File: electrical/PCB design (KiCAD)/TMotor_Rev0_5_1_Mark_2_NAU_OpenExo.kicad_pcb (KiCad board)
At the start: 2 copper layers, 89.4 x 82.6 mm, 96 parts, among them J1 Conn_01x07_Pin, J10 XT30PW-F, J11 XT30PW-F, J12 XT30PW-F, J13 TFM-107-01-L-D-WT, J2 Conn_01x04_Pin, J3 Conn_01x02_Pin, J4 Conn_01x02_Pin, J5 Conn_01x02_Pin, J6 Conn_01x02_Pin, J7 Conn_01x03_Pin, J8 XT30PW-F, J9 XT30PW-F, U1 TXU0104PWR, U10 DEV-16771, U2 TXU0304-Q1, U3 INA125U, U4 INA125U, U5 SN65HVD230DR, U6 INA125U, U7 INA125U

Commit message: design updates ; documentation update
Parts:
- removed the C19 at (157.9, 124.8)
- removed the C26 at (119.5, 71.7)
- removed the C3 at (151.7, 106.5)
- removed the D1 at (140.6, 121.3)
- removed D3, D4, D5: BAT54S, Package_TO_SOT_SMD:SOT-23
- removed INA_EXC_JP6, INA_EXC_JP7: SolderJumper_3_Open, Jumper:SolderJumper-3_P1.3mm_Open_RoundedPad1.0x1.5mm_NumberLabels
- removed J1: Conn_01x07_Pin, Connector_PinHeader_2.54mm:PinHeader_1x07_P2.54mm_Vertical
- removed J12: XT30PW-F, XT30PW-F:AMASS_XT30U-F_1x02_P5.0mm_Vertical
- removed the J4 at (136.6, 130.0)
- removed PS1: P78E05-1000, TMotor_Rev0_5_1_Mark_2_NAU_OpenExo:P78E05-1000
- removed the RIGHT_LC_CONN1 at (156.1, 69.9)
- removed U10: DEV-16771, TMotor_Rev0_5_1_Mark_2_NAU_OpenExo:MODULE_DEV-16771
- added C10: 22uF, Capacitor_SMD:C_0805_2012Metric_Pad1.18x1.45mm_HandSolder, B.Cu at (164.4, 117.0)
- added C11: 22uF, Capacitor_SMD:C_0805_2012Metric_Pad1.18x1.45mm_HandSolder, B.Cu at (164.4, 114.7)
- added C13: 100nF, Capacitor_SMD:C_0805_2012Metric_Pad1.18x1.45mm_HandSolder, F.Cu at (162.4, 132.5)
- added C23: 100nF, Capacitor_SMD:C_0805_2012Metric_Pad1.18x1.45mm_HandSolder, F.Cu at (144.5, 70.6)
- added C25: 1uF, Capacitor_SMD:C_0805_2012Metric_Pad1.18x1.45mm_HandSolder, F.Cu at (146.6, 70.6)
- added C28: 100nF, Capacitor_SMD:C_0805_2012Metric_Pad1.18x1.45mm_HandSolder, F.Cu at (124.0, 65.9)
- added C30: 1uF, Capacitor_SMD:C_0805_2012Metric_Pad1.18x1.45mm_HandSolder, F.Cu at (121.8, 65.9)
- added C32: 10nF, Capacitor_SMD:C_0805_2012Metric_Pad1.18x1.45mm_HandSolder, F.Cu at (152.3, 127.1)
- added C33: 10nF, Capacitor_SMD:C_0805_2012Metric_Pad1.18x1.45mm_HandSolder, F.Cu at (143.9, 111.7)
- added C34: 10nF, Capacitor_SMD:C_0805_2012Metric_Pad1.18x1.45mm_HandSolder, F.Cu at (141.2, 104.8)
- added C35: 10nF, Capacitor_SMD:C_0805_2012Metric_Pad1.18x1.45mm_HandSolder, F.Cu at (144.7, 99.5)
- added C36: 10nF, Capacitor_SMD:C_0805_2012Metric_Pad1.18x1.45mm_HandSolder, B.Cu at (155.3, 124.0)
- added C37: 10nF, Capacitor_SMD:C_0805_2012Metric_Pad1.18x1.45mm_HandSolder, F.Cu at (143.9, 109.5)
- added C38: 10nF, Capacitor_SMD:C_0805_2012Metric_Pad1.18x1.45mm_HandSolder, F.Cu at (142.6, 99.4)
- added C39: 10nF, Capacitor_SMD:C_0805_2012Metric_Pad1.18x1.45mm_HandSolder, F.Cu at (145.2, 95.2)
- added D10: BAS70-04, BAS70-04:P200_SOT-23, F.Cu at (152.7, 97.6)
- added D7: BAS70-04, BAS70-04:P200_SOT-23, B.Cu at (143.8, 117.0)
- added D8: BAS70-04, BAS70-04:P200_SOT-23, F.Cu at (150.9, 113.4)
- added D9: BAS70-04, BAS70-04:P200_SOT-23, F.Cu at (151.1, 108.5)
- added INA_EXC_JP1: SolderJumper_2_Open, Jumper:SolderJumper-2_P1.3mm_Open_RoundedPad1.0x1.5mm, F.Cu at (136.4, 134.2)
- added INA_EXC_JP2: SolderJumper_2_Open, Jumper:SolderJumper-2_P1.3mm_Open_RoundedPad1.0x1.5mm, F.Cu at (160.3, 126.5)
- added J7: XT30PW-F, XT30 new version:AMASS_XT30U-F_1x02_P5.0mm_Vertical, F.Cu at (182.4, 68.5)
- added R22: 1k, Resistor_SMD:R_0805_2012Metric_Pad1.20x1.40mm_HandSolder, B.Cu at (159.5, 124.0)
- added R23: 1k, Resistor_SMD:R_0805_2012Metric_Pad1.20x1.40mm_HandSolder, F.Cu at (133.8, 131.9)
- added R24: 1k, Resistor_SMD:R_0805_2012Metric_Pad1.20x1.40mm_HandSolder, B.Cu at (140.4, 84.2)
- added R25: 1k, Resistor_SMD:R_0805_2012Metric_Pad1.20x1.40mm_HandSolder, B.Cu at (125.3, 78.9)
- added RIGHT_LC_CONN2: TFM-107-01-L-D-WT, ISDF connector:SAMTEC_TFM-107-01-L-D-WT, F.Cu at (106.8, 114.5)
- added U7: DEV-16771, TEENSY:MODULE_DEV-16771, F.Cu at (120.2, 104.5)
- added U9: WPME-FDSM_SIP-3, 173010535:WPME-FDSM_17301XX35, F.Cu at (163.0, 113.0)
- C1: renamed from C6; footprint Capacitor_THT:C_Disc_D10.5mm_W5.0mm_P5.00mm -> Capacitor_SMD:C_0805_2012Metric_Pad1.18x1.45mm_HandSolder; moved to B.Cu
- C14: renamed from C24; footprint Capacitor_THT:C_Disc_D10.5mm_W5.0mm_P5.00mm -> Capacitor_SMD:C_0805_2012Metric_Pad1.18x1.45mm_HandSolder; moved to B.Cu
- C15: value 100nF -> 1uF; footprint Capacitor_THT:C_Disc_D10.5mm_W5.0mm_P5.00mm -> Capacitor_SMD:C_0805_2012Metric_Pad1.18x1.45mm_HandSolder
- C16: renamed from C25; footprint Capacitor_THT:C_Disc_D10.5mm_W5.0mm_P5.00mm -> Capacitor_SMD:C_0805_2012Metric_Pad1.18x1.45mm_HandSolder; moved to B.Cu
- C18, C2: footprint Capacitor_THT:C_Disc_D10.5mm_W5.0mm_P5.00mm -> Capacitor_SMD:C_0805_2012Metric_Pad1.18x1.45mm_HandSolder; moved to B.Cu
- C19: renamed from C21; footprint Capacitor_THT:C_Disc_D10.5mm_W5.0mm_P5.00mm -> Capacitor_SMD:C_0805_2012Metric_Pad1.18x1.45mm_HandSolder
- C20: value 100nF -> 1uF; footprint Capacitor_THT:C_Disc_D10.5mm_W5.0mm_P5.00mm -> Capacitor_SMD:C_0805_2012Metric_Pad1.18x1.45mm_HandSolder; moved to B.Cu
- C21: renamed from C22; footprint Capacitor_THT:C_Disc_D10.5mm_W5.0mm_P5.00mm -> Capacitor_SMD:C_0805_2012Metric_Pad1.18x1.45mm_HandSolder; moved to B.Cu
- C24: renamed from C27; footprint Capacitor_THT:C_Disc_D10.5mm_W5.0mm_P5.00mm -> Capacitor_SMD:C_0805_2012Metric_Pad1.18x1.45mm_HandSolder
- C26: renamed from C29; footprint Capacitor_THT:C_Disc_D10.5mm_W5.0mm_P5.00mm -> Capacitor_SMD:C_0805_2012Metric_Pad1.18x1.45mm_HandSolder
- C29: renamed from C28; footprint Capacitor_THT:C_Disc_D10.5mm_W5.0mm_P5.00mm -> Capacitor_SMD:C_0805_2012Metric_Pad1.18x1.45mm_HandSolder
- C3: renamed from C8; footprint Capacitor_THT:C_Disc_D10.5mm_W5.0mm_P5.00mm -> Capacitor_SMD:C_0805_2012Metric_Pad1.18x1.45mm_HandSolder; moved to B.Cu
- C31: renamed from C30; footprint Capacitor_THT:C_Disc_D10.5mm_W5.0mm_P5.00mm -> Capacitor_SMD:C_0805_2012Metric_Pad1.18x1.45mm_HandSolder
- C4: renamed from C7; footprint Capacitor_THT:C_Disc_D10.5mm_W5.0mm_P5.00mm -> Capacitor_SMD:C_0805_2012Metric_Pad1.18x1.45mm_HandSolder; moved to B.Cu
- C5: renamed from C23; footprint Capacitor_THT:C_Disc_D10.5mm_W5.0mm_P5.00mm -> Capacitor_SMD:C_0805_2012Metric_Pad1.18x1.45mm_HandSolder; moved to B.Cu
- C6: renamed from C5; footprint Capacitor_THT:C_Disc_D10.5mm_W5.0mm_P5.00mm -> Capacitor_SMD:C_0805_2012Metric_Pad1.18x1.45mm_HandSolder; moved to B.Cu
- C7: renamed from C9; footprint Capacitor_THT:C_Disc_D10.5mm_W5.0mm_P5.00mm -> Capacitor_SMD:C_0805_2012Metric_Pad1.18x1.45mm_HandSolder; moved to B.Cu
- C9: renamed from C4; footprint Capacitor_THT:C_Disc_D10.5mm_W5.0mm_P5.00mm -> Capacitor_SMD:C_0805_2012Metric_Pad1.18x1.45mm_HandSolder; moved to B.Cu
- INA_EXC_JP3, INA_EXC_JP4: value SolderJumper_3_Open -> SolderJumper_2_Open; footprint Jumper:SolderJumper-3_P1.3mm_Open_RoundedPad1.0x1.5mm_NumberLabels -> Jumper:SolderJumper-2_P1.3mm_Open_RoundedPad1.0x1.5mm
- INA_PWR_JP4: moved to F.Cu
- J10, J11, J8, J9: footprint XT30PW-F:AMASS_XT30U-F_1x02_P5.0mm_Vertical -> XT30 new version:AMASS_XT30U-F_1x02_P5.0mm_Vertical
- LEFT_LC_CONN1: value CONN_04X2 -> TFM-107-01-L-D-WT; footprint Connector_PinHeader_2.54mm:PinHeader_2x04_P2.54mm_Vertical -> ISDF connector:SAMTEC_TFM-107-01-L-D-WT
- R1: renamed from R12; footprint Resistor_THT:R_Axial_DIN0207_L6.3mm_D2.5mm_P10.16mm_Horizontal -> Resistor_SMD:R_0805_2012Metric_Pad1.20x1.40mm_HandSolder; moved to B.Cu
- R10: renamed from R4; value 4.7k -> 1k; footprint Resistor_THT:R_Axial_DIN0207_L6.3mm_D2.5mm_P10.16mm_Horizontal -> Resistor_SMD:R_0805_2012Metric_Pad1.20x1.40mm_HandSolder; moved to B.Cu
- R11: renamed from R15; value 10R -> 50; footprint Resistor_THT:R_Axial_DIN0207_L6.3mm_D2.5mm_P10.16mm_Horizontal -> Resistor_SMD:R_0805_2012Metric_Pad1.20x1.40mm_HandSolder
- R12: renamed from R20; value 1M -> 100k; footprint Resistor_THT:R_Axial_DIN0207_L6.3mm_D2.5mm_P10.16mm_Horizontal -> Resistor_SMD:R_0805_2012Metric_Pad1.20x1.40mm_HandSolder; moved to B.Cu
- R13: renamed from R24; value 1M -> 100k; footprint Resistor_THT:R_Axial_DIN0207_L6.3mm_D2.5mm_P10.16mm_Horizontal -> Resistor_SMD:R_0805_2012Metric_Pad1.20x1.40mm_HandSolder
- R14: renamed from R5; value 4.7k -> 1k; footprint Resistor_THT:R_Axial_DIN0207_L6.3mm_D2.5mm_P10.16mm_Horizontal -> Resistor_SMD:R_0805_2012Metric_Pad1.20x1.40mm_HandSolder; moved to B.Cu
- R15: renamed from R17; value 10R -> 50; footprint Resistor_THT:R_Axial_DIN0207_L6.3mm_D2.5mm_P10.16mm_Horizontal -> Resistor_SMD:R_0805_2012Metric_Pad1.20x1.40mm_HandSolder; moved to B.Cu
- R16: renamed from R21; value 1M -> 100k; footprint Resistor_THT:R_Axial_DIN0207_L6.3mm_D2.5mm_P10.16mm_Horizontal -> Resistor_SMD:R_0805_2012Metric_Pad1.20x1.40mm_HandSolder
- R17: renamed from R25; value 1M -> 100k; footprint Resistor_THT:R_Axial_DIN0207_L6.3mm_D2.5mm_P10.16mm_Horizontal -> Resistor_SMD:R_0805_2012Metric_Pad1.20x1.40mm_HandSolder
- R18: renamed from R6; value 4.7k -> 1k; footprint Resistor_THT:R_Axial_DIN0207_L6.3mm_D2.5mm_P10.16mm_Horizontal -> Resistor_SMD:R_0805_2012Metric_Pad1.20x1.40mm_HandSolder; moved to B.Cu
- R19: renamed from R18; value 10R -> 50; footprint Resistor_THT:R_Axial_DIN0207_L6.3mm_D2.5mm_P10.16mm_Horizontal -> Resistor_SMD:R_0805_2012Metric_Pad1.20x1.40mm_HandSolder; moved to B.Cu
- R2: renamed from R1; footprint Resistor_THT:R_Axial_DIN0207_L6.3mm_D2.5mm_P10.16mm_Horizontal -> Resistor_SMD:R_0805_2012Metric_Pad1.20x1.40mm_HandSolder; moved to B.Cu
- R20: renamed from R22; value 1M -> 100k; footprint Resistor_THT:R_Axial_DIN0207_L6.3mm_D2.5mm_P10.16mm_Horizontal -> Resistor_SMD:R_0805_2012Metric_Pad1.20x1.40mm_HandSolder
- R21: renamed from R26; value 1M -> 100k; footprint Resistor_THT:R_Axial_DIN0207_L6.3mm_D2.5mm_P10.16mm_Horizontal -> Resistor_SMD:R_0805_2012Metric_Pad1.20x1.40mm_HandSolder
- R3: renamed from R2; value 10R -> 10; footprint Resistor_THT:R_Axial_DIN0207_L6.3mm_D2.5mm_P10.16mm_Horizontal -> Resistor_SMD:R_0805_2012Metric_Pad1.20x1.40mm_HandSolder
- R4: renamed from R11; footprint Resistor_THT:R_Axial_DIN0207_L6.3mm_D2.5mm_P10.16mm_Horizontal -> Resistor_SMD:R_0805_2012Metric_Pad1.20x1.40mm_HandSolder
- R5: renamed from R7; footprint Resistor_THT:R_Axial_DIN0207_L6.3mm_D2.5mm_P10.16mm_Horizontal -> Resistor_SMD:R_0805_2012Metric_Pad1.20x1.40mm_HandSolder
- R6: renamed from R3; value 4.7k -> 1k; footprint Resistor_THT:R_Axial_DIN0207_L6.3mm_D2.5mm_P10.16mm_Horizontal -> Resistor_SMD:R_0805_2012Metric_Pad1.20x1.40mm_HandSolder
- R7: renamed from R16; value 10R -> 50; footprint Resistor_THT:R_Axial_DIN0207_L6.3mm_D2.5mm_P10.16mm_Horizontal -> Resistor_SMD:R_0805_2012Metric_Pad1.20x1.40mm_HandSolder; moved to B.Cu
- R8: renamed from R19; value 1M -> 100k; footprint Resistor_THT:R_Axial_DIN0207_L6.3mm_D2.5mm_P10.16mm_Horizontal -> Resistor_SMD:R_0805_2012Metric_Pad1.20x1.40mm_HandSolder; moved to B.Cu
- R9: renamed from R23; value 1M -> 100k; footprint Resistor_THT:R_Axial_DIN0207_L6.3mm_D2.5mm_P10.16mm_Horizontal -> Resistor_SMD:R_0805_2012Metric_Pad1.20x1.40mm_HandSolder; moved to B.Cu
- moved RIGHT_LC_CONN1 87.6 mm to (160.0, 67.6)
- moved C20 73.2 mm to (134.1, 142.6), turned to -90 degrees
- moved INA_EXC_JP3 66.9 mm to (136.3, 73.3)
- moved J9 48.6 mm to (184.1, 117.1)
- moved R8 43.1 mm to (162.1, 138.6), turned to 0 degrees
- moved C15 23.5 mm to (162.0, 136.4), turned to 180 degrees
- moved R11 23.1 mm to (145.5, 140.9), turned to -90 degrees
- moved R21 23.0 mm to (137.6, 69.5), turned to 0 degrees
- moved R20 22.8 mm to (137.6, 66.1), turned to 0 degrees
- moved R17 20.7 mm to (157.0, 72.8), turned to 0 degrees
- moved C3 20.2 mm to (124.4, 107.8), turned to -90 degrees
- moved J10 20.0 mm to (189.3, 136.3)
- moved R5 19.3 mm to (147.4, 130.2)
- moved R13 19.0 mm to (147.6, 144.1), turned to -90 degrees
- moved C18 16.9 mm to (134.2, 138.2), turned to 90 degrees
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- renumbered C1 to C8, D2 to D1, D6 to D2, INA219 to INA1, INA_PWR_JP3 to INA_PWR_JP1, INA_PWR_JP6 to INA_PWR_JP2, INA_PWR_JP7 to INA_PWR_JP3, INA_VREF_JP3 to INA_VREF_JP1, INA_VREF_JP6 to INA_VREF_JP2, INA_VREF_JP7 to INA_VREF_JP3, J6 to J3, J5 to J4, J3 to J5, J7 to J6, J13 to RIGHT_LC_CONN1, SHUNT0 to SHUNT1, TP2 to TP1, TP1 to TP2, U$6 to U$1, U3 to U1, U6 to U2, U7 to U3, U1 to U5, U2 to U6, U5 to U8
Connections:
- A1 pad D0: /MCUs/NANO_RX -> /MCUs/NANO_TX
- C14 pad 1: /Load cells/Left LC Amplifier 2/Vbridge- -> /Load cells/Left LC Amplifier 2 (label 2)/Vbridge-
- C15 pad 1: Net-(PS1-GND/-VOUT) -> Net-(INA_PWR_JP2-C)
- C16 pad 1: /Load cells/Left LC Amplifier 2/Vbridge+ -> /Load cells/Left LC Amplifier 2 (label 2)/Vbridge+
- C18 pad 1: Net-(U3-SENSE) (its old number) -> Net-(INA_PWR_JP1-C)
- C19 pad 1: /Load cells/Left LC  Amplifier 1/Vbridge- -> /Load cells/Left LC  Amplifier 1 (label 1)/Vbridge-
- C20 pad 1: Net-(U4-SENSE) -> Net-(INA_PWR_JP1-C)
- C21 pad 1: /Load cells/Left LC  Amplifier 1/Vbridge+ -> /Load cells/Left LC  Amplifier 1 (label 1)/Vbridge+
- C24 pad 1: /Load cells/Right LC  Amplifier 2/Vbridge- -> /Load cells/Right LC  Amplifier 2 (label 4)/Vbridge-
- C26 pad 1: /Load cells/Right LC  Amplifier 2/Vbridge+ -> /Load cells/Right LC  Amplifier 2 (label 4)/Vbridge+
- C29 pad 1: /Load cells/Right LC Amplifier 1/Vbridge- -> /Load cells/Right LC Amplifier 1 (label 3)/Vbridge-
- C31 pad 1: /Load cells/Right LC Amplifier 1/Vbridge+ -> /Load cells/Right LC Amplifier 1 (label 3)/Vbridge+
- INA_EXC_JP3 pad 1: +5V -> Net-(INA_EXC_JP3-A)
- INA_EXC_JP3 pad 2: L1_LC_P -> Net-(INA_EXC_JP3-B)
- INA_EXC_JP4 pad 1: +5V -> Net-(INA_EXC_JP4-A)
- INA_EXC_JP4 pad 2: R2_LC_P -> Net-(INA_EXC_JP4-B)
- INA_PWR_JP1 pad 2: Net-(INA_PWR_JP3-C) (its old number) -> Net-(INA_PWR_JP1-C)
- INA_PWR_JP2 pad 2: Net-(INA_PWR_JP6-C) -> Net-(INA_PWR_JP2-C)
- INA_VREF_JP1 pad 2: Net-(INA_EXC_JP3-B) -> Net-(INA_EXC_JP1-A)
- INA_VREF_JP3 pad 2: Net-(INA_EXC_JP7-B) -> Net-(INA_EXC_JP3-A)
- INA_VREF_JP4 pad 2: Net-(INA_EXC_JP4-B) -> Net-(INA_EXC_JP4-A)
- J10 pad 1: (no net) -> GND
- J10 pad 2: (no net) -> /CAN and peripherals./VBATT
- J11 pad 1: (no net) -> GND
- J11 pad 2: (no net) -> /CAN and peripherals./VBATT
- J8 pad 1: (no net) -> GND
- J8 pad 2: (no net) -> /CAN and peripherals./VBATT
- J9 pad 1: (no net) -> GND
- J9 pad 2: (no net) -> /CAN and peripherals./VBATT
- R10 pad 1: Net-(U3-SENSE) (its old number) -> Net-(U1-SENSE)
- R12 pad 1: /Load cells/Left LC  Amplifier 1/Vbridge+ -> /Load cells/Left LC  Amplifier 1 (label 1)/Vbridge+
- R13 pad 1: /Load cells/Left LC  Amplifier 1/Vbridge- -> /Load cells/Left LC  Amplifier 1 (label 1)/Vbridge-
- R16 pad 1: /Load cells/Right LC  Amplifier 2/Vbridge+ -> /Load cells/Right LC  Amplifier 2 (label 4)/Vbridge+
- R17 pad 1: /Load cells/Right LC  Amplifier 2/Vbridge- -> /Load cells/Right LC  Amplifier 2 (label 4)/Vbridge-
- R20 pad 1: /Load cells/Right LC Amplifier 1/Vbridge+ -> /Load cells/Right LC Amplifier 1 (label 3)/Vbridge+
- R21 pad 1: /Load cells/Right LC Amplifier 1/Vbridge- -> /Load cells/Right LC Amplifier 1 (label 3)/Vbridge-
- R8 pad 1: /Load cells/Left LC Amplifier 2/Vbridge+ -> /Load cells/Left LC Amplifier 2 (label 2)/Vbridge+
- R9 pad 1: /Load cells/Left LC Amplifier 2/Vbridge- -> /Load cells/Left LC Amplifier 2 (label 2)/Vbridge-
- RIGHT_LC_CONN1 pad 01: unconnected-(J13-Pad01) -> /Load cells/Right LC  Amplifier 2 (label 4)/Vbridge+
- RIGHT_LC_CONN1 pad 02: unconnected-(J13-Pad02) -> /Load cells/Right LC Amplifier 1 (label 3)/Vbridge-
- RIGHT_LC_CONN1 pad 03: unconnected-(J13-Pad03) -> /Load cells/Right LC  Amplifier 2 (label 4)/Vbridge-
- RIGHT_LC_CONN1 pad 04: unconnected-(J13-Pad04) -> /Load cells/Right LC Amplifier 1 (label 3)/Vbridge+
- RIGHT_LC_CONN1 pad 05: unconnected-(J13-Pad05) -> +5V
- RIGHT_LC_CONN1 pad 06: unconnected-(J13-Pad06) -> GND
- RIGHT_LC_CONN1 pad 07: unconnected-(J13-Pad07) -> +5V
- RIGHT_LC_CONN1 pad 08: unconnected-(J13-Pad08) -> GND
- TeensyPowerJP1 pad 1: +5V -> Net-(TeensyPowerJP1-A)
- TeensyPowerJP1 pad 2: Net-(TeensyPowerJP1-B) -> +5V
- U$1 pad 1: Net-(PS1-GND/-VOUT) -> Net-(U$1-P$1)
- U1 pad 1: Net-(INA_PWR_JP3-C) (its old number) -> Net-(INA_PWR_JP1-C)
- U1 pad 10: Net-(U3-SENSE) (its old number) -> Net-(U1-SENSE)
- U1 pad 11: Net-(U3-SENSE) (its old number) -> Net-(U1-SENSE)
- U1 pad 2: Net-(INA_PWR_JP3-C) (its old number) -> Net-(INA_PWR_JP1-C)
- U1 pad 4: Net-(INA_EXC_JP3-B) -> Net-(INA_EXC_JP1-A)
- U1 pad 5: Net-(INA_EXC_JP3-B) -> Net-(INA_EXC_JP1-A)
- U1 pad 6: /Load cells/Left LC  Amplifier 1/Vbridge+ -> /Load cells/Left LC  Amplifier 1 (label 1)/Vbridge+
- U1 pad 7: /Load cells/Left LC  Amplifier 1/Vbridge- -> /Load cells/Left LC  Amplifier 1 (label 1)/Vbridge-
- U2 pad 1: Net-(INA_PWR_JP6-C) -> Net-(INA_PWR_JP2-C)
- U2 pad 2: Net-(INA_PWR_JP6-C) -> Net-(INA_PWR_JP2-C)
- U2 pad 6: /Load cells/Left LC Amplifier 2/Vbridge+ -> /Load cells/Left LC Amplifier 2 (label 2)/Vbridge+
- U2 pad 7: /Load cells/Left LC Amplifier 2/Vbridge- -> /Load cells/Left LC Amplifier 2 (label 2)/Vbridge-
- U3 pad 4: Net-(INA_EXC_JP7-B) -> Net-(INA_EXC_JP3-A)
- U3 pad 5: Net-(INA_EXC_JP7-B) -> Net-(INA_EXC_JP3-A)
- U3 pad 6: /Load cells/Right LC Amplifier 1/Vbridge+ -> /Load cells/Right LC Amplifier 1 (label 3)/Vbridge+
- U3 pad 7: /Load cells/Right LC Amplifier 1/Vbridge- -> /Load cells/Right LC Amplifier 1 (label 3)/Vbridge-
- U4 pad 4: Net-(INA_EXC_JP4-B) -> Net-(INA_EXC_JP4-A)
- U4 pad 5: Net-(INA_EXC_JP4-B) -> Net-(INA_EXC_JP4-A)
- U4 pad 6: /Load cells/Right LC  Amplifier 2/Vbridge+ -> /Load cells/Right LC  Amplifier 2 (label 4)/Vbridge+
- U4 pad 7: /Load cells/Right LC  Amplifier 2/Vbridge- -> /Load cells/Right LC  Amplifier 2 (label 4)/Vbridge-
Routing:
- net /Load cells/Right LC Amplifier 1/Vbridge+: track 55.2 -> 0.00 mm, vias 2 -> 0
- net /Load cells/Right LC Amplifier 1/Vbridge-: track 52.1 -> 0.00 mm, vias 1 -> 0
- net /Load cells/Left LC Amplifier 2/Vbridge+: track 50.9 -> 0.00 mm
- net /Load cells/Left LC  Amplifier 1/Vbridge+: track 47.8 -> 0.00 mm, vias 1 -> 0
- net /Load cells/Left LC  Amplifier 1/Vbridge-: track 42.4 -> 0.00 mm, vias 1 -> 0
- net /Load cells/Right LC  Amplifier 2/Vbridge-: track 35.6 -> 0.00 mm, vias 1 -> 0
- net /Load cells/Right LC Amplifier 1 (label 3)/Vbridge+: track 0.00 -> 32.9 mm, vias 0 -> 1
- net /Load cells/Right LC  Amplifier 2/Vbridge+: track 32.9 -> 0.00 mm, vias 1 -> 0
- net /Load cells/Right LC Amplifier 1 (label 3)/Vbridge-: track 0.00 -> 29.7 mm, vias 0 -> 1
- net Net-(U3-SENSE) (its old number): track 26.8 -> 0.00 mm, vias 1 -> 0
- net /Load cells/Left LC Amplifier 2/Vbridge-: track 22.0 -> 0.00 mm
- net R2_LC_P: track 50.2 -> 28.5 mm
- net /Load cells/Left LC  Amplifier 1 (label 1)/Vbridge-: track 0.00 -> 21.6 mm, vias 0 -> 1
- net /Load cells/Left LC  Amplifier 1 (label 1)/Vbridge+: track 0.00 -> 20.9 mm, vias 0 -> 3
- net SYNC_DEFAULT: track 20.1 -> 0.00 mm
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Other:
- board text added: "AnkleExo Board v1.1.1 McGill NeuroC Lab (2026)"
- board text added: "INA_PWR"
- board text added: "SPI"
- board text removed: "AnkleExo Board v1.1.0 McGill NeuroC Lab (2026)"
- board text removed: "CIPO"
- board text removed: "COPI"
- board text removed: "CS1"
- board text removed: "CS2"
- board text removed: "INAPwr"
- board text removed: "INARef"
- board text removed: "SCK"
- board text removed: "SPIx2"

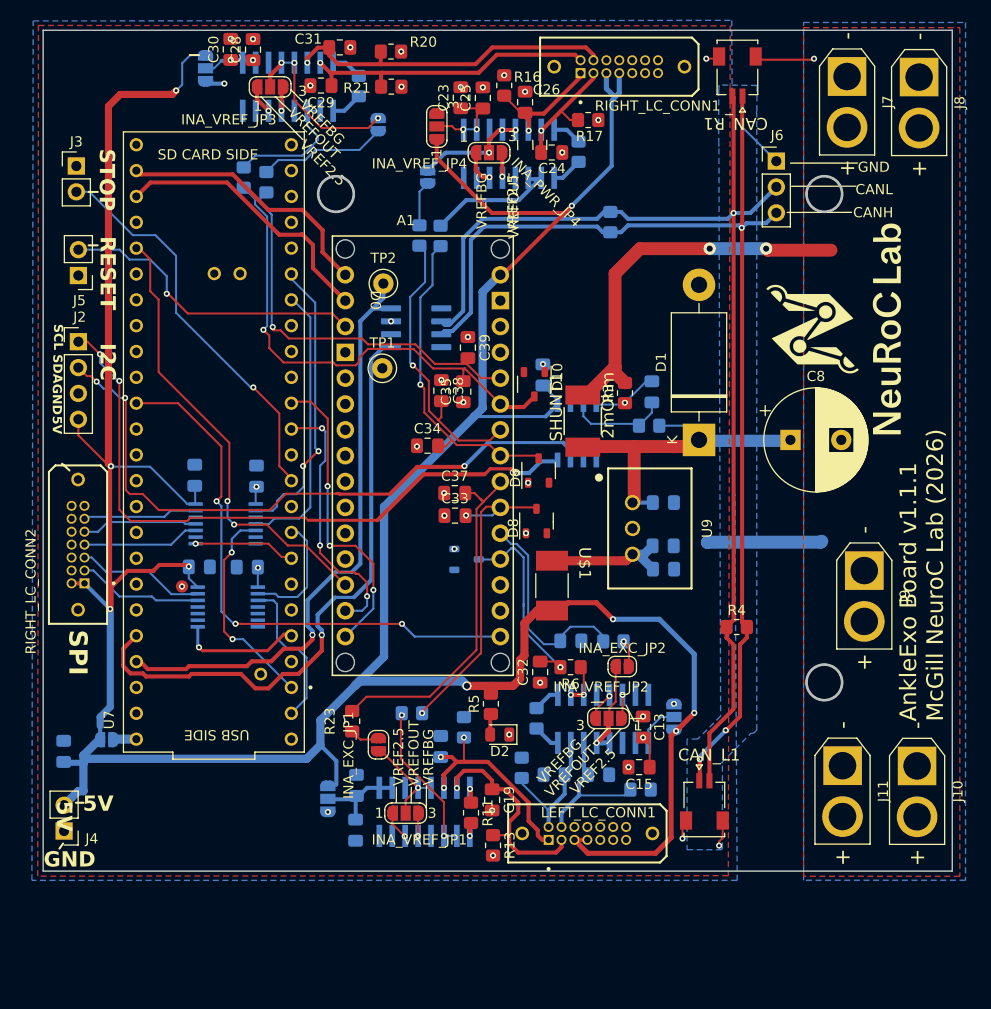
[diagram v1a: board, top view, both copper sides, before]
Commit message: updated ble and uart
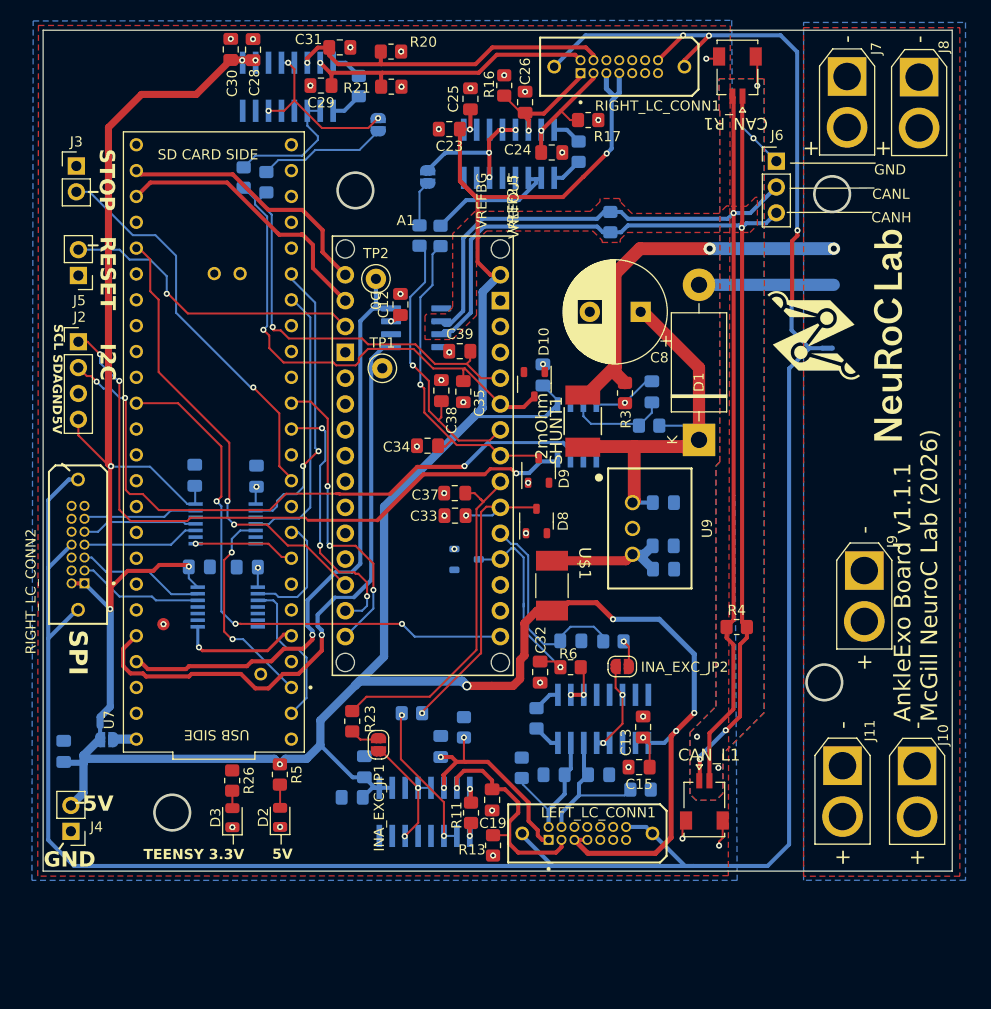
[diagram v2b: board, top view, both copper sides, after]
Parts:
- removed INA_PWR_JP1, INA_PWR_JP2, INA_PWR_JP3, INA_PWR_JP4, INA_VREF_JP1, INA_VREF_JP2, INA_VREF_JP3, INA_VREF_JP4: SolderJumper_3_Open, Jumper:SolderJumper-3_P1.3mm_Open_RoundedPad1.0x1.5mm_NumberLabels
- added C12: 100nF, Capacitor_SMD:C_0805_2012Metric_Pad1.18x1.45mm_HandSolder, F.Cu at (138.5, 90.9)
- added D3: LED, LED_SMD:LED_0805_2012Metric, F.Cu at (122.0, 141.4)
- added NT1: NetTie_2, NetTie:NetTie-2_SMD_Pad0.5mm, B.Cu at (180.5, 95.2)
- added R26: 470, Resistor_SMD:R_0805_2012Metric_Pad1.20x1.40mm_HandSolder, F.Cu at (122.0, 137.7)
- R5: value 600kR -> 1k
- moved D2 23.1 mm to (126.7, 141.4), turned to 90 degrees
- moved R5 21.9 mm to (126.7, 137.1), turned to -90 degrees
- moved C8 19.4 mm to (162.1, 91.7), turned to 180 degrees
- moved C20 6.29 mm to (135.0, 136.4), turned to 90 degrees
- moved C23 3.28 mm to (143.3, 73.7), turned to 180 degrees
- moved C18 1.25 mm to (133.8, 139.4), turned to 180 degrees
- moved C25 1.22 mm to (145.4, 70.7)
- moved C39 0.87 mm to (144.4, 95.5), turned to 0 degrees
- moved TP2 0.86 mm to (136.1, 88.4)
- moved J4 0.67 mm to (106.1, 142.7)
- moved G*** 0.62 mm to (181.6, 94.0)
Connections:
- C13 pad 1: Net-(INA_PWR_JP2-C) -> +5V
- C15 pad 1: Net-(INA_PWR_JP2-C) -> +5V
- C18 pad 1: Net-(INA_PWR_JP1-C) -> +5V
- C20 pad 1: Net-(INA_PWR_JP1-C) -> +5V
- C23 pad 1: Net-(INA_PWR_JP4-C) -> +5V
- C25 pad 1: Net-(INA_PWR_JP4-C) -> +5V
- C28 pad 1: Net-(INA_PWR_JP3-C) -> +5V
- C30 pad 1: Net-(INA_PWR_JP3-C) -> +5V
- LEFT_LC_CONN1 pad 14: unconnected-(LEFT_LC_CONN1-Pad14) -> SHIELD
- LEFT_LC_CONN1 pad S1: (no net) -> SHIELD
- LEFT_LC_CONN1 pad S2: (no net) -> SHIELD
- R5 pad 1: Net-(D2-A) -> +5V
- R5 pad 2: +5V -> Net-(D2-A)
- RIGHT_LC_CONN1 pad 14: unconnected-(RIGHT_LC_CONN1-Pad14) -> SHIELD
- RIGHT_LC_CONN1 pad S1: (no net) -> SHIELD
- RIGHT_LC_CONN1 pad S2: (no net) -> SHIELD
- RIGHT_LC_CONN2 pad 08: unconnected-(RIGHT_LC_CONN2-Pad08) -> SHIELD
- RIGHT_LC_CONN2 pad S1: (no net) -> SHIELD
- RIGHT_LC_CONN2 pad S2: (no net) -> SHIELD
- U1 pad 1: Net-(INA_PWR_JP1-C) -> +5V
- U1 pad 13: Net-(INA_VREF_JP1-B) -> unconnected-(U1-VREFBG-Pad13)
- U1 pad 14: Net-(INA_VREF_JP1-A) -> Net-(INA_EXC_JP1-A)
- U1 pad 2: Net-(INA_PWR_JP1-C) -> +5V
- U2 pad 1: Net-(INA_PWR_JP2-C) -> +5V
- U2 pad 13: Net-(INA_VREF_JP2-B) -> unconnected-(U2-VREFBG-Pad13)
- U2 pad 14: Net-(INA_VREF_JP2-A) -> Net-(INA_EXC_JP2-A)
- U2 pad 2: Net-(INA_PWR_JP2-C) -> +5V
- U3 pad 1: Net-(INA_PWR_JP3-C) -> +5V
- U3 pad 13: Net-(INA_VREF_JP3-B) -> unconnected-(U3-VREFBG-Pad13)
- U3 pad 14: Net-(INA_VREF_JP3-A) -> Net-(INA_EXC_JP3-A)
- U3 pad 2: Net-(INA_PWR_JP3-C) -> +5V
- U4 pad 1: Net-(INA_PWR_JP4-C) -> +5V
- U4 pad 13: Net-(INA_VREF_JP4-B) -> unconnected-(U4-VREFBG-Pad13)
- U4 pad 14: Net-(INA_VREF_JP4-A) -> Net-(INA_EXC_JP4-A)
- U4 pad 2: Net-(INA_PWR_JP4-C) -> +5V
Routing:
- net SHIELD: track 0.00 -> 246.8 mm, vias 0 -> 4
- net +5V: track 330.0 -> 350.4 mm, vias 9 -> 13
- net Net-(INA_PWR_JP2-C): track 9.22 -> 0.00 mm, vias 1 -> 0
- net Net-(INA_PWR_JP1-C): track 8.82 -> 0.00 mm
- net Net-(INA_PWR_JP4-C): track 8.54 -> 0.00 mm, vias 2 -> 0
- net /CAN and peripherals./L7_VIN: track 33.5 -> 41.1 mm
- net Net-(INA_PWR_JP3-C): track 5.37 -> 0.00 mm, vias 2 -> 0
- net Net-(INA_VREF_JP4-A): track 3.36 -> 0.00 mm, vias 1 -> 0
- net Net-(INA_VREF_JP3-A): track 2.82 -> 0.00 mm, vias 1 -> 0
- net Net-(INA_VREF_JP1-A): track 2.78 -> 0.00 mm, vias 1 -> 0
- net Net-(INA_VREF_JP2-B): track 2.74 -> 0.00 mm, vias 1 -> 0
- net Net-(INA_EXC_JP4-A): track 11.0 -> 13.4 mm, vias 3 -> 4
- net Net-(INA_VREF_JP3-B): track 2.43 -> 0.00 mm, vias 1 -> 0
- net Net-(INA_VREF_JP4-B): track 2.35 -> 0.00 mm, vias 1 -> 0
- net Net-(INA_VREF_JP2-A): track 2.33 -> 0.00 mm, vias 1 -> 0
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- added copper zone on F.Cu, net GND
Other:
- outline, holes or cut-outs redrawn
- board text added: "TEENSY 3.3V"
- board text removed: "3.3V"
- board text removed: "3V3"
- board text removed: "INA125 V+"
- board text removed: "INA_PWR"
- board text removed: "INA_pwr"

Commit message: fix modularize python script for ble.py and sensors.py (main and plotting-csv not done
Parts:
- removed INA1: ~, TMotor_Rev0_5_1_Mark_2_NAU_OpenExo:D8_TEX
- removed J6: Conn_01x03_Pin, Connector_PinHeader_2.54mm:PinHeader_1x03_P2.54mm_Vertical
- added C17: 0.1uF, Capacitor_SMD:C_0805_2012Metric_Pad1.18x1.45mm_HandSolder, B.Cu at (160.2, 104.5)
- added C22: 0.1uF, Capacitor_SMD:C_0805_2012Metric_Pad1.18x1.45mm_HandSolder, F.Cu at (166.4, 76.0)
- added C27: 10nF, Capacitor_SMD:C_0805_2012Metric_Pad1.18x1.45mm_HandSolder, F.Cu at (121.1, 85.5)
- added C40: 10nF, Capacitor_SMD:C_0805_2012Metric_Pad1.18x1.45mm_HandSolder, F.Cu at (121.2, 83.5)
- added J1: Conn_02x03_Counter_Clockwise, Connector_PinHeader_2.54mm:PinHeader_2x03_P2.54mm_Vertical, F.Cu at (174.9, 77.7)
- added JP1: SolderJumper_3_Open, Jumper:SolderJumper-3_P1.3mm_Open_RoundedPad1.0x1.5mm, B.Cu at (168.8, 70.4)
- added JP2: SolderJumper_3_Open, Jumper:SolderJumper-3_P1.3mm_Open_RoundedPad1.0x1.5mm, B.Cu at (150.9, 66.8)
- added R27: 3.3k, Resistor_SMD:R_0805_2012Metric_Pad1.20x1.40mm_HandSolder, B.Cu at (151.8, 102.7)
- added R28: 3.3k, Resistor_SMD:R_0805_2012Metric_Pad1.20x1.40mm_HandSolder, B.Cu at (151.8, 104.8)
- added R29: 10k, Resistor_THT:R_Axial_DIN0207_L6.3mm_D2.5mm_P7.62mm_Horizontal, F.Cu at (163.3, 72.3)
- added R30: 10k, Resistor_THT:R_Axial_DIN0207_L6.3mm_D2.5mm_P7.62mm_Horizontal, F.Cu at (166.4, 72.3)
- added R31: 1k, Resistor_SMD:R_0805_2012Metric_Pad1.20x1.40mm_HandSolder, B.Cu at (125.9, 86.8)
- added R32: 1k, Resistor_SMD:R_0805_2012Metric_Pad1.20x1.40mm_HandSolder, B.Cu at (123.9, 85.1)
- added U10: INA232AIDDFR, INA232AIDDFR:SOT_32AIDDFR_TEX, B.Cu at (156.4, 102.4)
- C6: value 100nF -> 0.1uF; moved to F.Cu
- C7: value 100nF -> 0.1uF
- R2: value 10R -> 10
- moved C6 24.5 mm to (163.3, 75.9), turned to -90 degrees
- moved R2 0.55 mm to (163.5, 102.8)
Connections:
- C6 pad 1: +5V -> FSR_2_IN
- RIGHT_LC_CONN1 pad 10: unconnected-(RIGHT_LC_CONN1-Pad10) -> /Load cells/FSR1/Vexcitation
- RIGHT_LC_CONN1 pad 11: unconnected-(RIGHT_LC_CONN1-Pad11) -> FSR_2_IN
- RIGHT_LC_CONN1 pad 12: unconnected-(RIGHT_LC_CONN1-Pad12) -> FSR_1_IN
- RIGHT_LC_CONN1 pad 13: unconnected-(RIGHT_LC_CONN1-Pad13) -> /Load cells/FSR2/Vexcitation
- U7 pad 18: unconnected-(U7-A4-Pad18) -> SDA
- U7 pad 19: unconnected-(U7-A5-Pad19) -> SCL
- U7 pad 24: unconnected-(U7-A10-Pad24) -> Net-(U7-A10)
- U7 pad 25: unconnected-(U7-A11-Pad25) -> Net-(U7-A11)
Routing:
- net FSR_1_IN: track 0.00 -> 63.0 mm
- net FSR_2_IN: track 0.00 -> 53.2 mm
- net Net-(U7-A10): track 0.00 -> 13.2 mm, vias 0 -> 1
- net /Load cells/FSR1/Vexcitation: track 0.00 -> 12.6 mm, vias 0 -> 1
- net Net-(U7-A11): track 0.00 -> 12.6 mm, vias 0 -> 1
- net +3V3: track 4.49 -> 11.7 mm, vias 4 -> 9
- net SCL: track 65.0 -> 72.2 mm
- net /Load cells/FSR2/Vexcitation: track 0.00 -> 5.95 mm, vias 0 -> 1
- net GND: track 27.6 -> 33.0 mm, vias 37 -> 41
- net +5V: track 350.4 -> 354.6 mm, vias 13 -> 14
- net R1_LC_P: track 39.9 -> 43.5 mm
- net SDA: track 63.5 -> 66.7 mm
- net R1_LC_N: track 48.9 -> 51.5 mm
- net Net-(U10-IN-): track 9.76 -> 7.66 mm
- net /CAN and peripherals./CAN_P: track 113.0 -> 114.6 mm
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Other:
- outline, holes or cut-outs redrawn

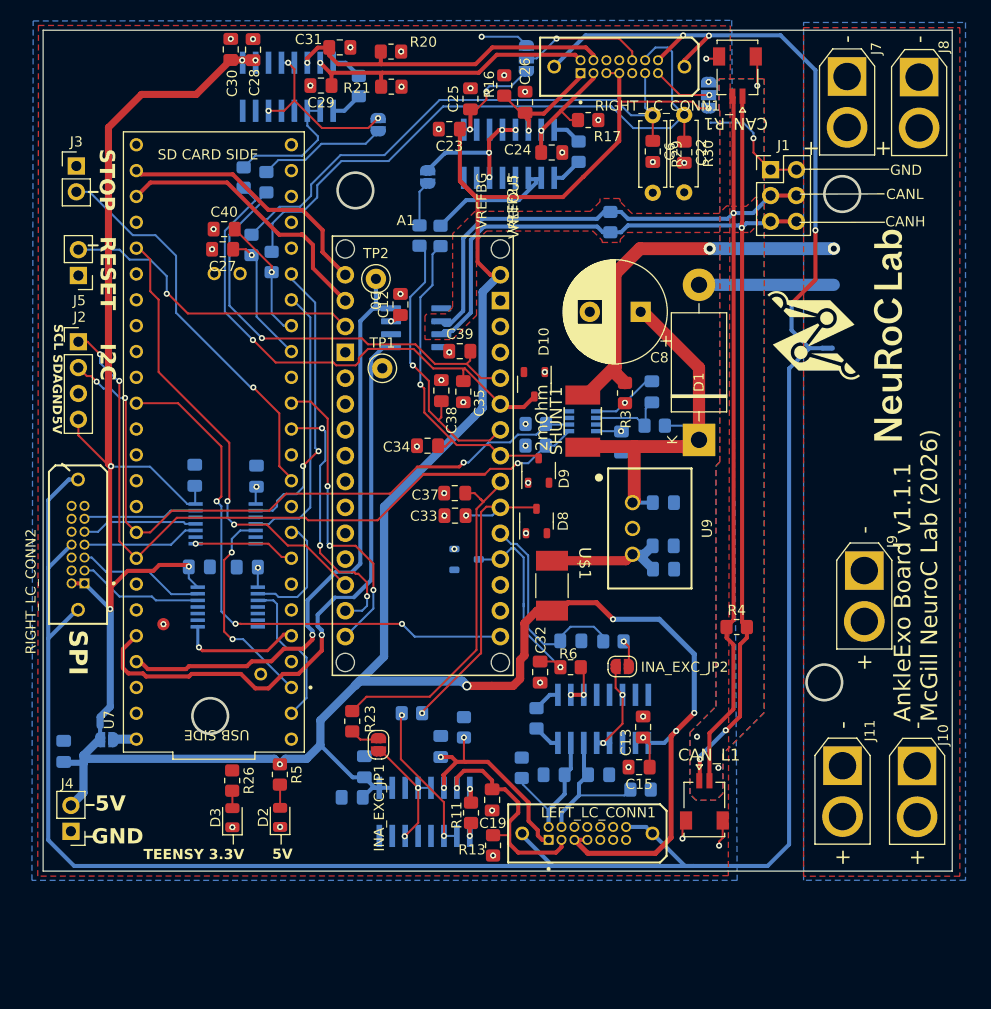
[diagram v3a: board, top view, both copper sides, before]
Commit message: fixed singleLeg python scripts
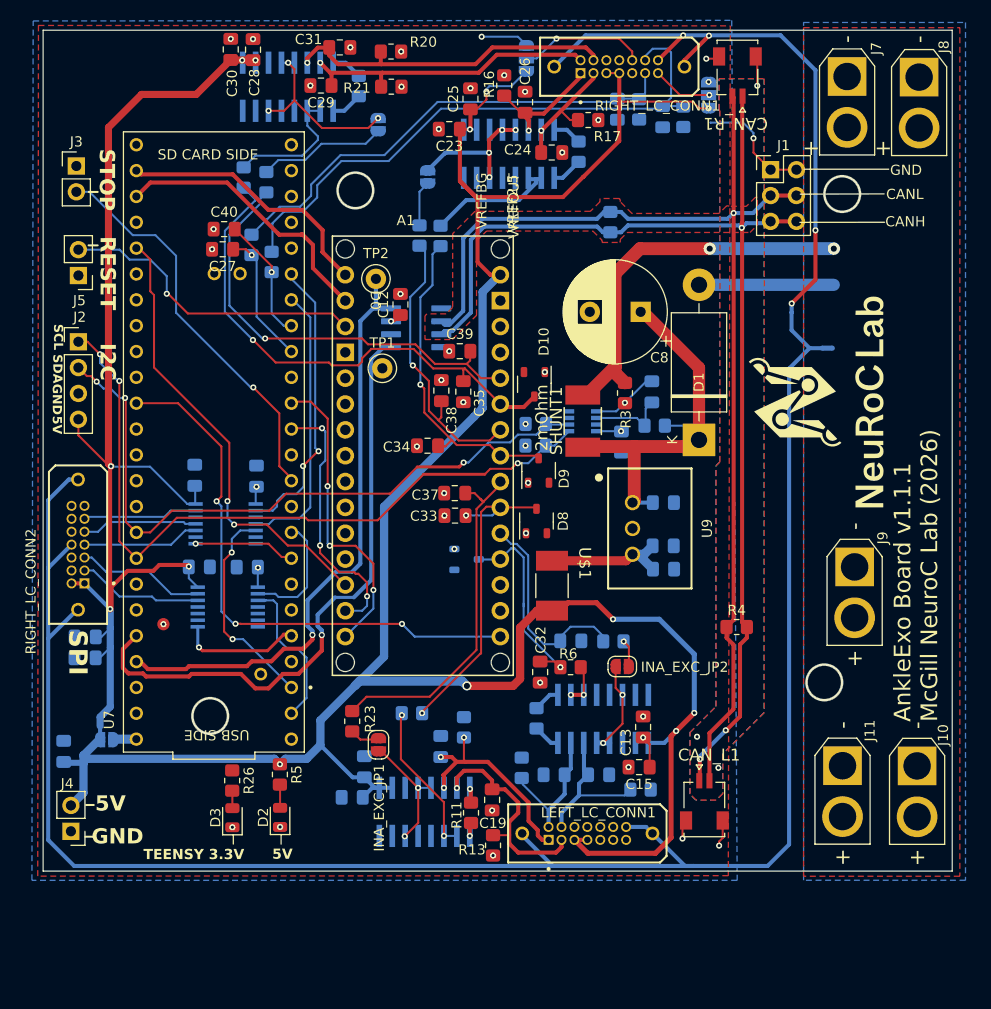
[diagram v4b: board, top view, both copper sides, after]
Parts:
- added C43: 0.1uF, Capacitor_SMD:C_0805_2012Metric_Pad1.18x1.45mm_HandSolder, B.Cu at (107.5, 123.6)
- added C44: 10uF, Capacitor_SMD:C_0805_2012Metric_Pad1.18x1.45mm_HandSolder, B.Cu at (107.5, 125.7)
- C22, C6: moved to B.Cu
- R29, R30: footprint Resistor_THT:R_Axial_DIN0207_L6.3mm_D2.5mm_P7.62mm_Horizontal -> Resistor_SMD:R_0805_2012Metric_Pad1.20x1.40mm_HandSolder; moved to B.Cu
- moved G*** 6.82 mm to (179.8, 100.6)
- moved C6 5.42 mm to (159.8, 71.7)
- moved C22 4.09 mm to (164.3, 72.5)
- moved R29 1.46 mm to (162.0, 71.8)
- moved J9 1.02 mm to (183.2, 116.7)
- moved R30 0.21 mm to (166.3, 72.5)
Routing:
- net FSR_1_IN: track 63.0 -> 57.7 mm
- net FSR_2_IN: track 53.2 -> 47.9 mm
- net +5V: track 354.6 -> 358.2 mm
- net GND: vias 41 -> 39
